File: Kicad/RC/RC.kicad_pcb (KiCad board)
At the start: 2 copper layers, 20 x 55 mm, 4 parts, among them SW1 SW_Push, SW2 SW_Wuerth_450301014042

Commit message: label update
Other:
- board text added: "+"
- board text added: "-"
- board text added: "OFF"
- board text added: "ON"
- board text added: "slow-mo"
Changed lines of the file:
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@@
 		(layer "Edge.Cuts")
+	)
+	(gr_text "reverse engineering by na103\ngithub.com/na103/bbar3"
+		(at 140.5 93 -90)
+		(layer "B.SilkS")
+		(effects
+			(font
+				(size 1 1)
+				(thickness 0.1)
+			)
+			(justify left bottom mirror)
+		)
+	)
+	(gr_text "+"
+		(at 157 110 0)
+		(layer "F.SilkS")
+		(effects
+			(font
+				(size 2 2)
+				(thickness 0.25)
+			)
+			(justify bottom)
+		)
+	)
+	(gr_text "slow-mo"
+		(at 146 86 0)
+		(layer "F.SilkS")
+		(effects
+			(font
+				(size 1 1)
+				(thickness 0.1)
+			)
+			(justify left bottom)
+		)
+	)
+	(gr_text "-"
+		(at 142 110 0)
+		(layer "F.SilkS")
+		(effects
+			(font
+				(size 2 2)
+				(thickness 0.25)
+			)
+			(justify bottom)
+		)
+	)
+	(gr_text "OFF"
+		(at 142.5 88 0)
+		(layer "F.SilkS")
+		(effects
+			(font
+				(size 2 2)
+				(thickness 0.25)
+			)
+			(justify bottom)
+		)
 	)
 	(gr_text "Amiga Action Replay\nremote control"
@@
 		)
 	)
-	(gr_text "reverse engineering by na103\ngithub.com/na103/bbar3"
-		(at 143 93 90)
+	(gr_text "ON"
+		(at 156.5 88 0)
 		(layer "F.SilkS")
 		(effects
 			(font
-				(size 1 1)
-				(thickness 0.1)
+				(size 2 2)
+				(thickness 0.25)
 			)
-			(justify left bottom)
+			(justify bottom)
 		)
 	)

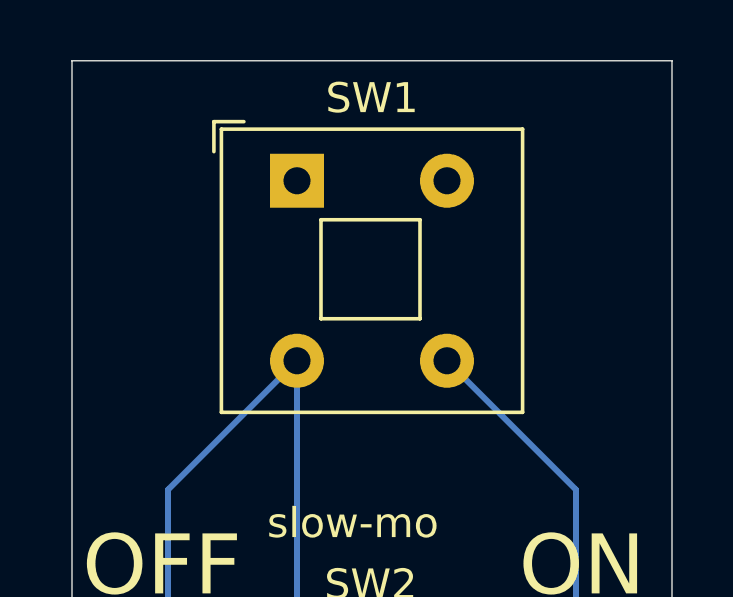
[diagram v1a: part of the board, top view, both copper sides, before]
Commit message: update SW1 footprint
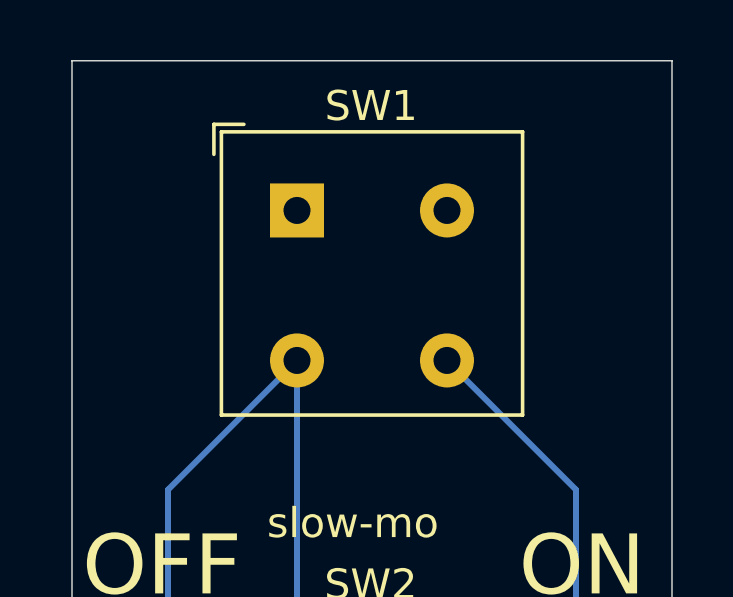
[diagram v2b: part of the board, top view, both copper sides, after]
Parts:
- SW1: footprint Button_Switch_THT:SW_Push_2P1T_Toggle_CK_PVA1xxH1xxxxxxV2 -> SamacSys_Parts:SW_Push_2P1T_Toggle_CK_PVA1xxH1xxxxxxV3
- moved SW1 0.99 mm to (147.0, 75.0)
